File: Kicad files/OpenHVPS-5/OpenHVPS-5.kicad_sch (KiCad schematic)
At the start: 79 parts, among them J1 Conn_01x03_Male, Q1 FQT7N10, Q2 BC846A, Q3 MMBT3906, Q4 MMBT3906, U1 MAX6008AEUR+T, U2 74HC14, U3 MAX4162, U4 CD14538BM

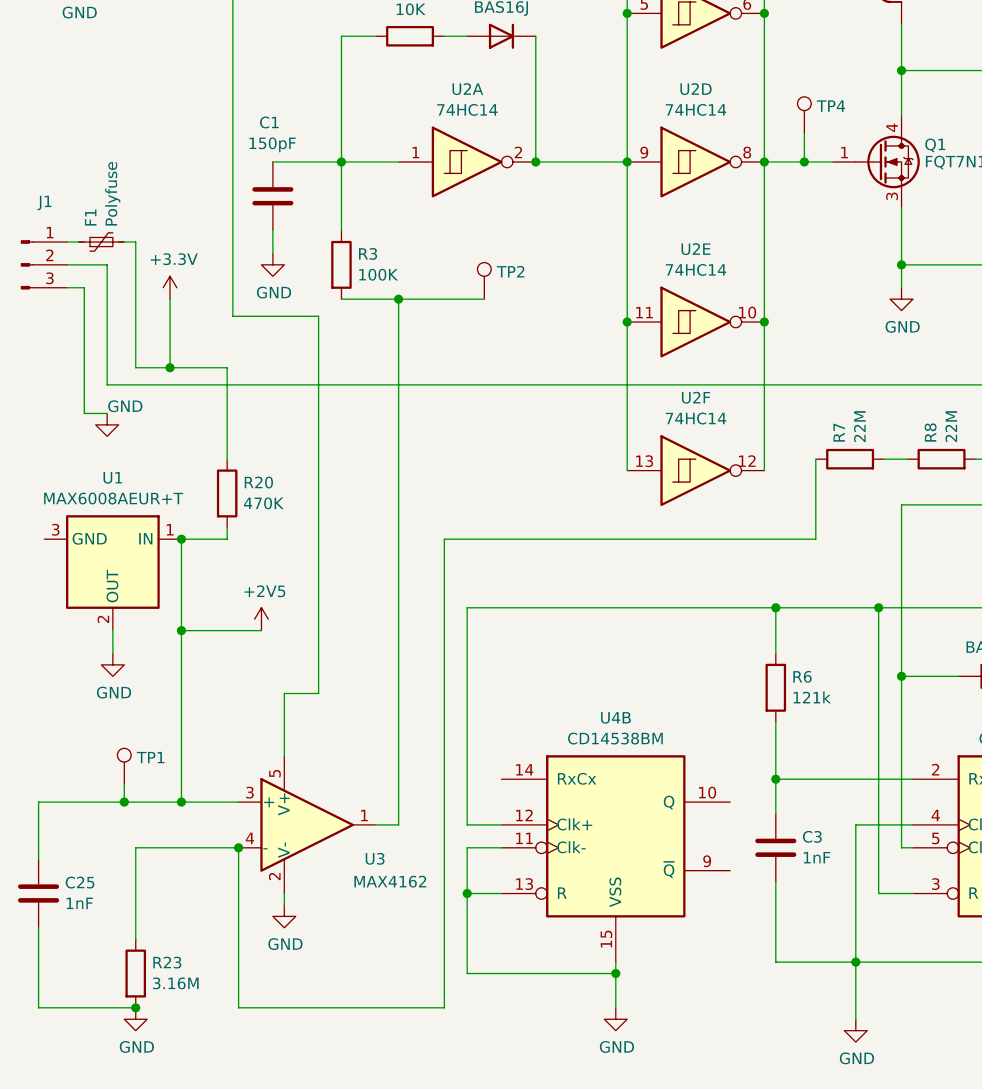
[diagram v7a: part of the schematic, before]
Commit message: Updated RC network around opamp and text changes.
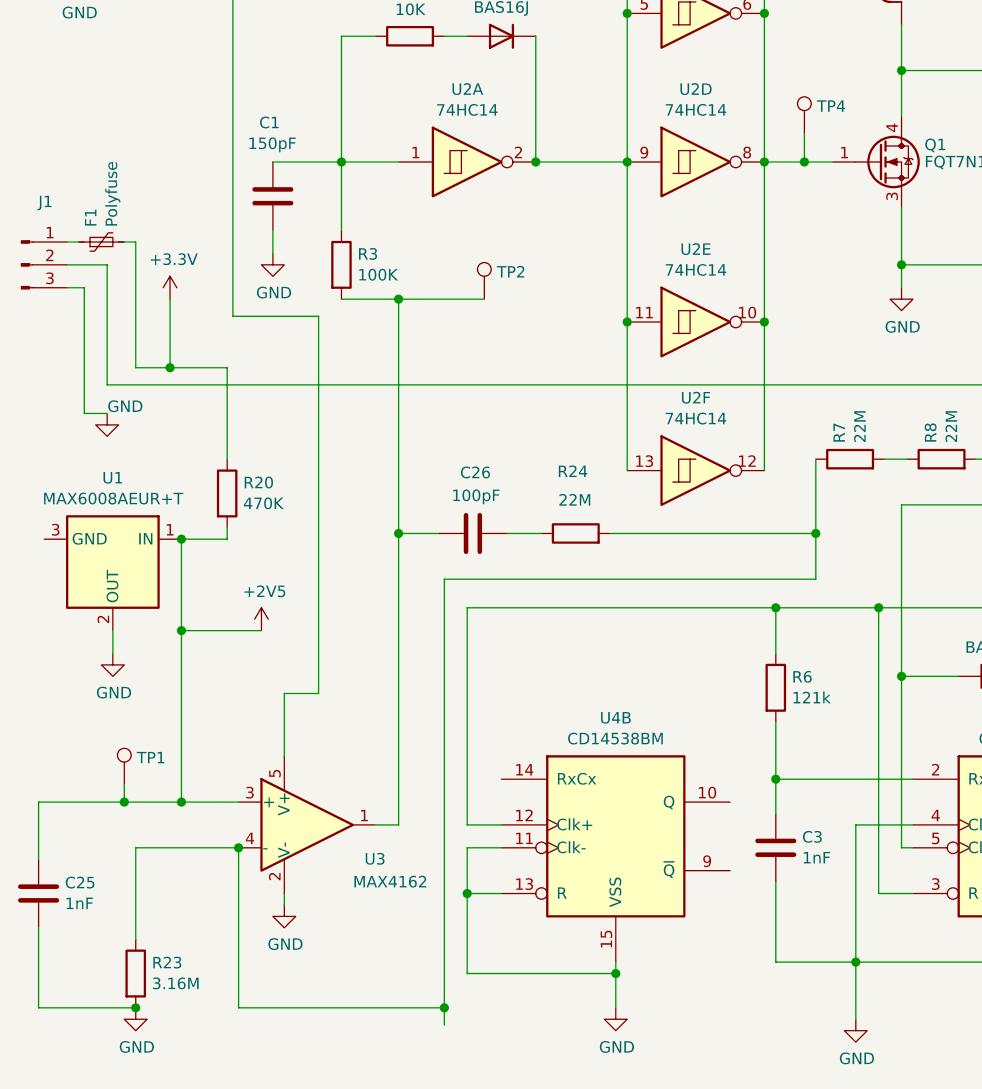
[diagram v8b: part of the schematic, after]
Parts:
- added C26: 100pF, Capacitor_SMD:C_0805_2012Metric, symbol Device:C
- added R24: 22M, Resistor_SMD:R_0805_2012Metric, symbol Device:R
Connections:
- net at R3.2, TP2.1, U3.1: now also C26.1
- net at R23.1, R7.1, U3.4 (-): now also R24.2
- new net: C26.2, R24.1
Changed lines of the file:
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@@
   (title_block
     (title "SafePulse")
-    (date "2021-02-10")
+    (date "2021-02-17")
     (rev "1.11")
     (company "SafeCast Team")
@@
   (junction (at 58.42 37.465) (diameter 1.016) (color 0 0 0 0))
   (junction (at 59.69 103.505) (diameter 1.016) (color 0 0 0 0))
+  (junction (at 59.69 129.54) (diameter 1.016) (color 0 0 0 0))
+  (junction (at 64.77 182.245) (diameter 1.016) (color 0 0 0 0))
   (junction (at 67.31 169.545) (diameter 1.016) (color 0 0 0 0))
   (junction (at 74.93 88.265) (diameter 1.016) (color 0 0 0 0))
@@
   (junction (at 102.87 20.955) (diameter 1.016) (color 0 0 0 0))
   (junction (at 104.775 88.265) (diameter 1.016) (color 0 0 0 0))
+  (junction (at 106.045 129.54) (diameter 1.016) (color 0 0 0 0))
   (junction (at 110.49 177.165) (diameter 1.016) (color 0 0 0 0))
   (junction (at 113.03 137.795) (diameter 1.016) (color 0 0 0 0))
@@
     (stroke (width 0) (type solid) (color 0 0 0 0))
   )
-  (wire (pts (xy 29.21 159.385) (xy 35.56 159.385))
-    (stroke (width 0) (type solid) (color 0 0 0 0))
-  )
   (wire (pts (xy 30.48 97.155) (xy 30.48 111.125))
     (stroke (width 0) (type solid) (color 0 0 0 0))
@@
     (stroke (width 0) (type solid) (color 0 0 0 0))
   )
-  (wire (pts (xy 35.56 140.335) (xy 35.56 159.385))
+  (wire (pts (xy 35.56 159.385) (xy 29.21 159.385))
+    (stroke (width 0) (type solid) (color 0 0 0 0))
+  )
+  (wire (pts (xy 35.56 159.385) (xy 35.56 140.335))
     (stroke (width 0) (type solid) (color 0 0 0 0))
   )
@@
     (stroke (width 0) (type solid) (color 0 0 0 0))
   )
+  (wire (pts (xy 59.69 103.505) (xy 59.69 129.54))
+    (stroke (width 0) (type solid) (color 0 0 0 0))
+  )
   (wire (pts (xy 59.69 103.505) (xy 69.215 103.505))
     (stroke (width 0) (type solid) (color 0 0 0 0))
   )
-  (wire (pts (xy 59.69 161.925) (xy 59.69 103.505))
+  (wire (pts (xy 59.69 129.54) (xy 59.69 161.925))
+    (stroke (width 0) (type solid) (color 0 0 0 0))
+  )
+  (wire (pts (xy 59.69 129.54) (xy 64.135 129.54))
     (stroke (width 0) (type solid) (color 0 0 0 0))
   )
@@
     (stroke (width 0) (type solid) (color 0 0 0 0))
   )
-  (wire (pts (xy 64.77 130.175) (xy 64.77 182.245))
-    (stroke (width 0) (type solid) (color 0 0 0 0))
-  )
-  (wire (pts (xy 64.77 130.175) (xy 106.045 130.175))
+  (wire (pts (xy 64.77 134.62) (xy 64.77 182.245))
+    (stroke (width 0) (type solid) (color 0 0 0 0))
+  )
+  (wire (pts (xy 64.77 134.62) (xy 106.045 134.62))
     (stroke (width 0) (type solid) (color 0 0 0 0))
   )
@@
     (stroke (width 0) (type solid) (color 0 0 0 0))
   )
+  (wire (pts (xy 64.77 182.245) (xy 64.77 184.15))
+    (stroke (width 0) (type solid) (color 0 0 0 0))
+  )
   (wire (pts (xy 67.31 37.465) (xy 58.42 37.465))
     (stroke (width 0) (type solid) (color 0 0 0 0))
@@
     (stroke (width 0) (type solid) (color 0 0 0 0))
   )
+  (wire (pts (xy 71.755 129.54) (xy 75.565 129.54))
+    (stroke (width 0) (type solid) (color 0 0 0 0))
+  )
   (wire (pts (xy 74.93 37.465) (xy 81.28 37.465))
     (stroke (width 0) (type solid) (color 0 0 0 0))
@@
     (stroke (width 0) (type solid) (color 0 0 0 0))
   )
+  (wire (pts (xy 83.185 129.54) (xy 106.045 129.54))
+    (stroke (width 0) (type solid) (color 0 0 0 0))
+  )
   (wire (pts (xy 83.82 178.435) (xy 83.82 177.165))
     (stroke (width 0) (type solid) (color 0 0 0 0))
@@
     (stroke (width 0) (type solid) (color 0 0 0 0))
   )
-  (wire (pts (xy 85.09 88.265) (xy 85.09 106.045))
+  (wire (pts (xy 85.09 106.045) (xy 85.09 88.265))
     (stroke (width 0) (type solid) (color 0 0 0 0))
   )
@@
     (stroke (width 0) (type solid) (color 0 0 0 0))
   )
-  (wire (pts (xy 106.045 130.175) (xy 106.045 121.285))
+  (wire (pts (xy 106.045 121.285) (xy 106.045 129.54))
+    (stroke (width 0) (type solid) (color 0 0 0 0))
+  )
+  (wire (pts (xy 106.045 129.54) (xy 106.045 134.62))
     (stroke (width 0) (type solid) (color 0 0 0 0))
   )
@@
     (pin "2")
   )
+  (symbol (lib_id "Device:R") (at 79.375 129.54 90) (unit 1)
+    (in_bom yes) (on_board yes)
+    (property "Reference" "R24" (id 0) (at 80.747 122.682 90)
+      (effects (font (size 1.27 1.27)) (justify left))
+    )
+    (property "Value" "22M" (id 1) (at 81.153 125.857 90)
+      (effects (font (size 1.27 1.27)) (justify left))
+    )
+    (property "Footprint" "Resistor_SMD:R_0805_2012Metric" (id 2) (at 79.375 131.318 90)
+      (effects (font (size 1.27 1.27)) hide)
+    )
+    (property "Datasheet" "https://www.digikey.com/en/products/detail/stackpole-electronics-inc/RMCF0805FT22M0/6053747" (id 3) (at 79.375 129.54 0)
+      (effects (font (size 1.27 1.27)) hide)
+    )
+    (pin "1")
+    (pin "2")
+  )
   (symbol (lib_id "Device:R") (at 101.6 146.685 0) (unit 1)
     (in_bom yes) (on_board yes)
@@
     )
     (property "Datasheet" "https://www.digikey.com/en/products/detail/samsung-electro-mechanics/CL21B105KOFNNNG/3894469" (id 3) (at 58.42 43.815 0)
+      (effects (font (size 1.27 1.27)) hide)
+    )
+    (pin "1")
+    (pin "2")
+  )
+  (symbol (lib_id "Device:C") (at 67.945 129.54 90) (unit 1)
+    (in_bom yes) (on_board yes)
+    (property "Reference" "C26" (id 0) (at 69.952 122.809 90)
+      (effects (font (size 1.27 1.27)) (justify left))
+    )
+    (property "Value" "100pF" (id 1) (at 70.993 125.349 90)
+      (effects (font (size 1.27 1.27)) (justify left))
+    )
+    (property "Footprint" "Capacitor_SMD:C_0805_2012Metric" (id 2) (at 71.755 128.575 0)
+      (effects (font (size 1.27 1.27)) hide)
+    )
+    (property "Datasheet" "https://www.digikey.com/en/products/detail/samsung-electro-mechanics/CL21C101JCANNNC/3886919" (id 3) (at 67.945 129.54 0)
       (effects (font (size 1.27 1.27)) hide)
     )
@@
       (reference "C25") (unit 1) (value "1nF") (footprint "Capacitor_SMD:C_0805_2012Metric")
     )
+    (path "/25bfefa3-d5bc-4056-80ac-9f7bceed815c"
+      (reference "C26") (unit 1) (value "100pF") (footprint "Capacitor_SMD:C_0805_2012Metric")
+    )
     (path "/00000000-0000-0000-0000-0000600ddc6a"
       (reference "D1") (unit 1) (value "BAS16J") (footprint "Diode_SMD:D_SOD-323")
@@
       (reference "R23") (unit 1) (value "3.16M") (footprint "Resistor_SMD:R_0805_2012Metric")
     )
+    (path "/95ffa48f-5e4a-4d1a-b1a7-fe360b6ab119"
+      (reference "R24") (unit 1) (value "22M") (footprint "Resistor_SMD:R_0805_2012Metric")
+    )
     (path "/a00aaed8-a3fc-4d63-a7e6-25589e061b4e"
